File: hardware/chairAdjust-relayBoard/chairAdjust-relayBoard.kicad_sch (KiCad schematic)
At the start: 51 parts, among them J1 Motor_1 + -, J2 Control-Signals, J3 Control-Signals, J4 24V Power, J5 GND Power, J6 12V, GND, J7 Motor_2 + -, K1 RT314A24, K2 RT314A24, K3 RT314A24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

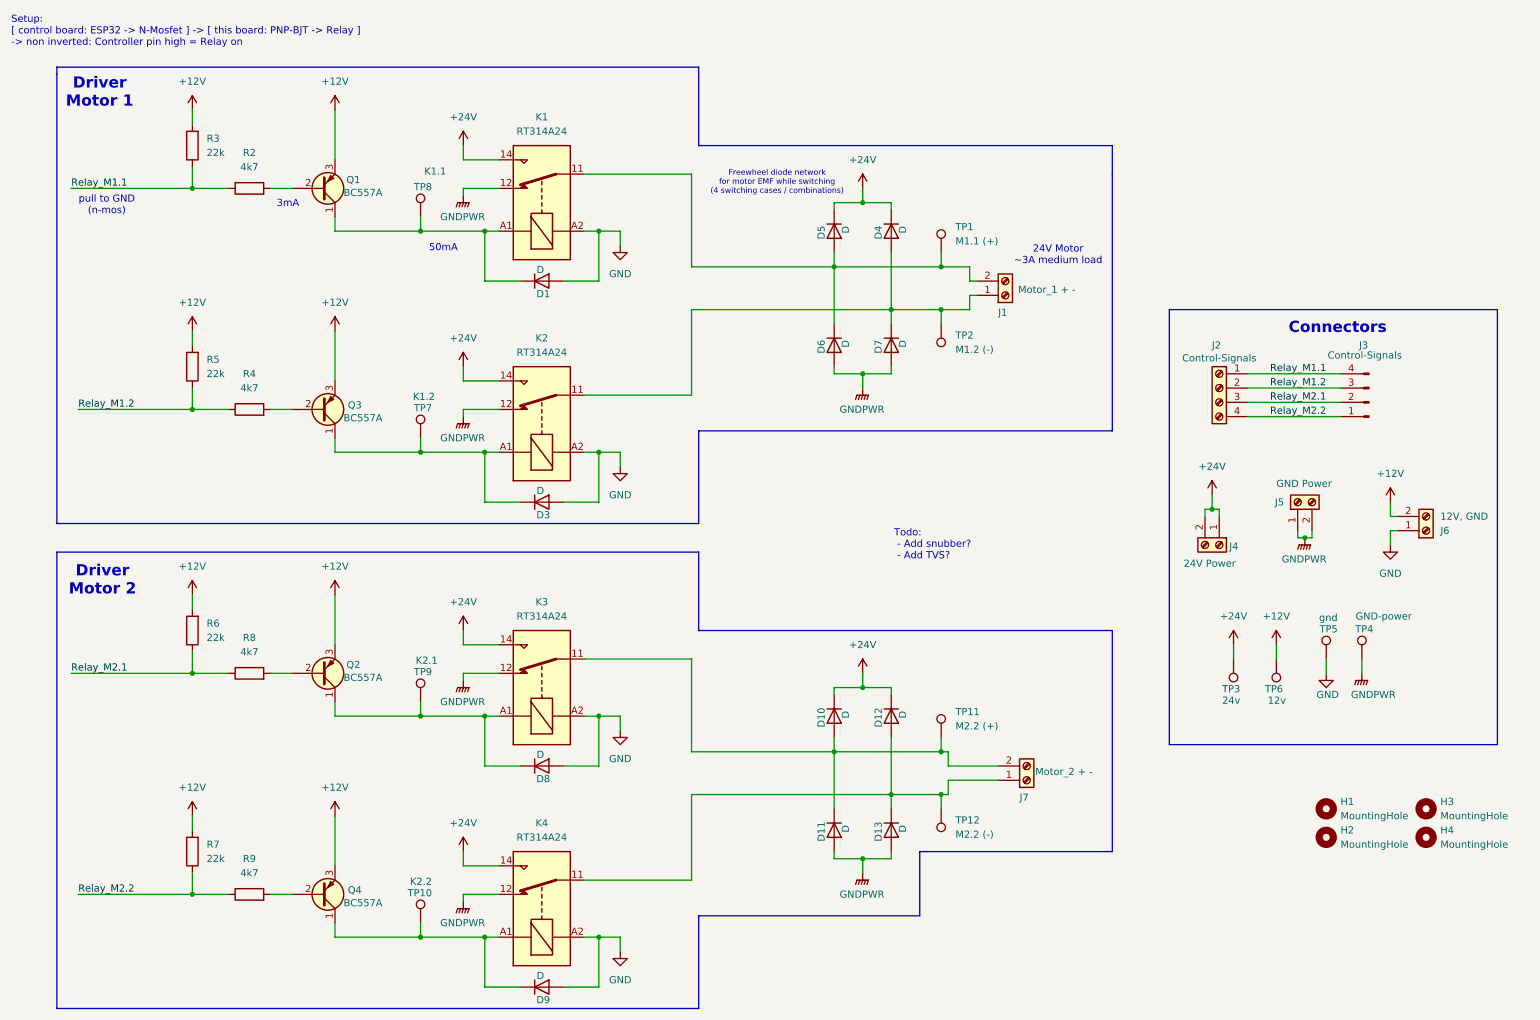
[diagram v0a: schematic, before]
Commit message: pcb: add 3d-model, exports
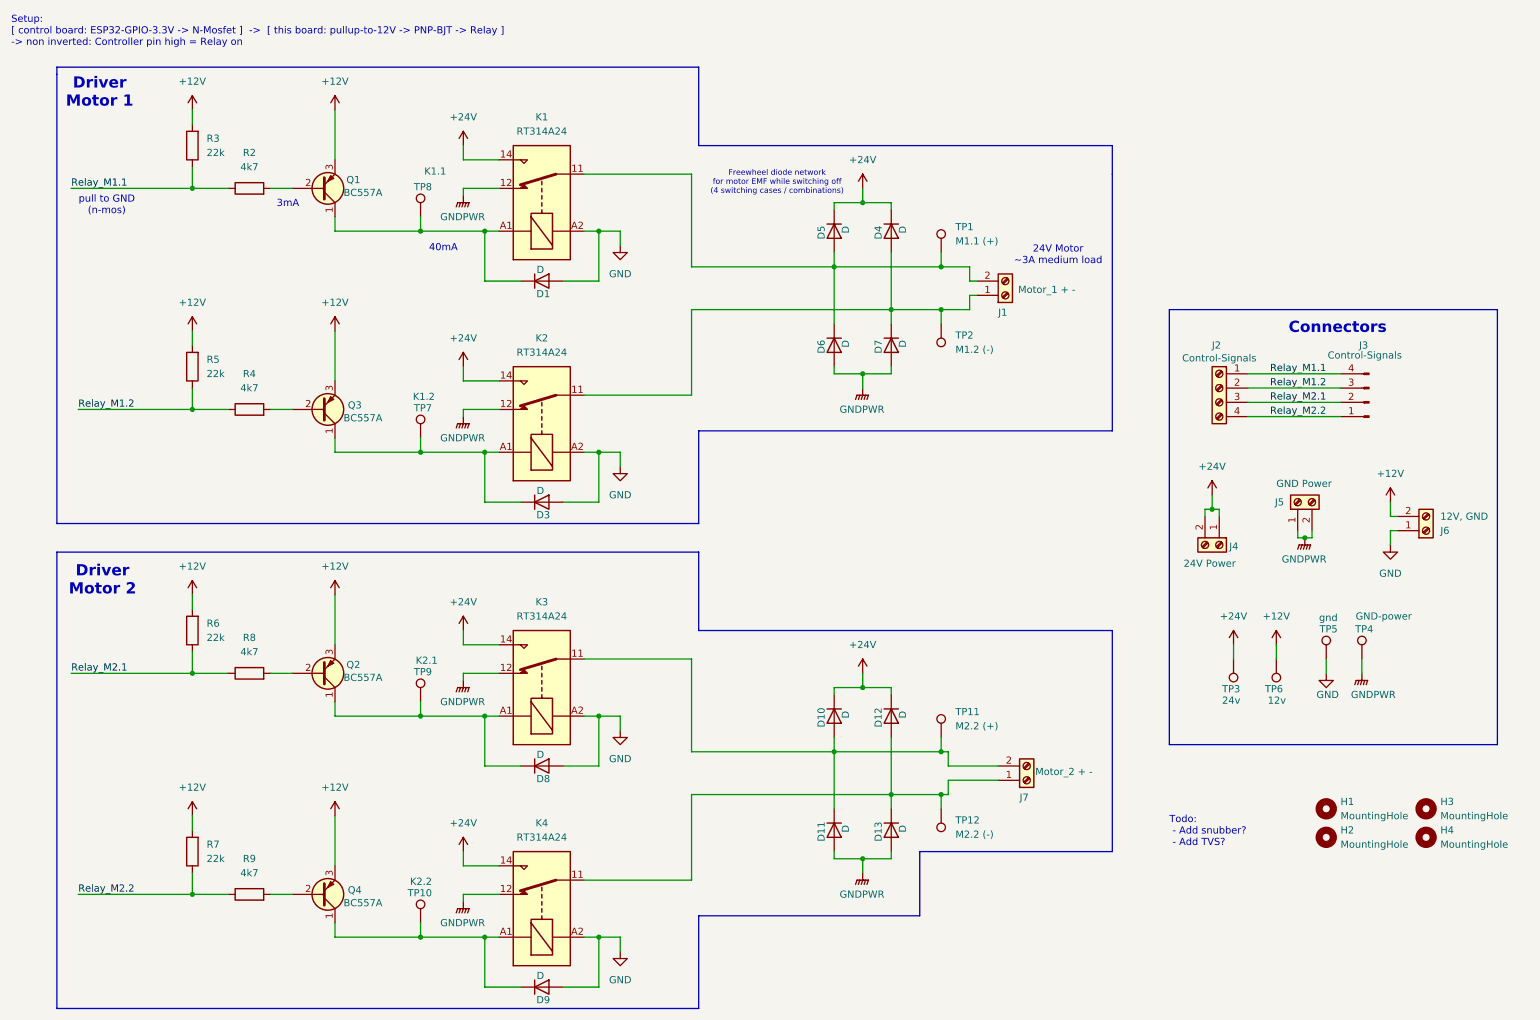
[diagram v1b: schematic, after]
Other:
- note added: "40mA"
- note added: "Freewheel diode network for motor EMF while switching off (4 switching cases / combinations)"
- note added: "Setup: [ control board: ESP32-GPIO-3.3V -> N-Mosfet ] -> [ this board: pullup-to-12V -> PNP-BJT -> Relay ] -> non inverted: Controller pin high = Relay on"
- note removed: "50mA"
- note removed: "Freewheel diode network for motor EMF while switching (4 switching cases / combinations)"
- note removed: "Setup: [ control board: ESP32 -> N-Mosfet ] -> [ this board: PNP-BJT -> Relay ] -> non inverted: Controller pin high = Relay on"
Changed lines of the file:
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@@
 		(date "2024-09-07")
 		(rev "V1.0")
-		(comment 1 "in both direction with protection")
-		(comment 2 "2 motors for chair adjust of armchair")
-		(comment 3 "Relay board for controlling ")
+		(comment 1 "https://github.com/Jonny999999/armchair_fw ")
+		(comment 2 "in both direction with protection")
+		(comment 3 "2 motors for chair adjustment of armchair")
+		(comment 4 "Relay board for controlling ")
 	)
 	(junction
@@
 		)
 	)
-	(text "Setup:\n[ control board: ESP32 -> N-Mosfet ] -> [ this board: PNP-BJT -> Relay ]\n-> non inverted: Controller pin high = Relay on"
+	(text "Setup:\n[ control board: ESP32-GPIO-3.3V -> N-Mosfet ]  ->  [ this board: pullup-to-12V -> PNP-BJT -> Relay ]\n-> non inverted: Controller pin high = Relay on"
 		(exclude_from_sim no)
 		(at 13.462 16.51 0)
@@
 		)
 	)
-	(text "50mA\n"
+	(text "40mA\n"
 		(exclude_from_sim no)
 		(at 90.424 55.118 0)
@@
 	(text "Todo: \n - Add snubber?\n - Add TVS?"
 		(exclude_from_sim no)
-		(at 170.688 107.95 0)
+		(at 219.71 159.004 0)
 		(effects
 			(font
@@
 		)
 	)
-	(text "Freewheel diode network\nfor motor EMF while switching\n(4 switching cases / combinations)"
+	(text "Freewheel diode network\nfor motor EMF while switching off\n(4 switching cases / combinations)"
 		(exclude_from_sim no)
 		(at 149.86 43.434 0)

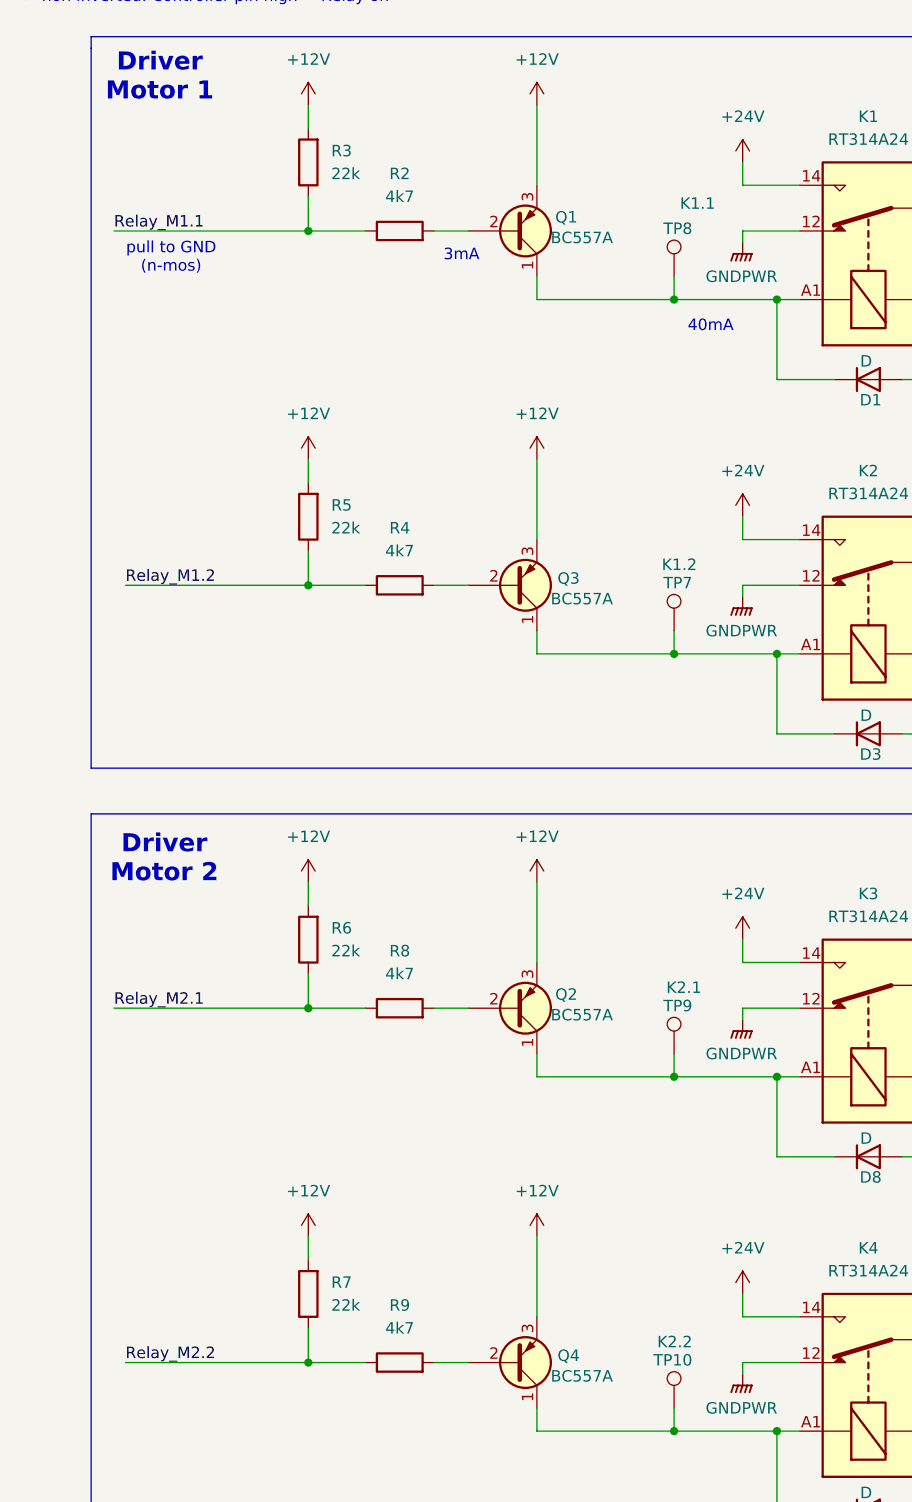
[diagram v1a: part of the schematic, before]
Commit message: Finalize schematic, Add pcb to README
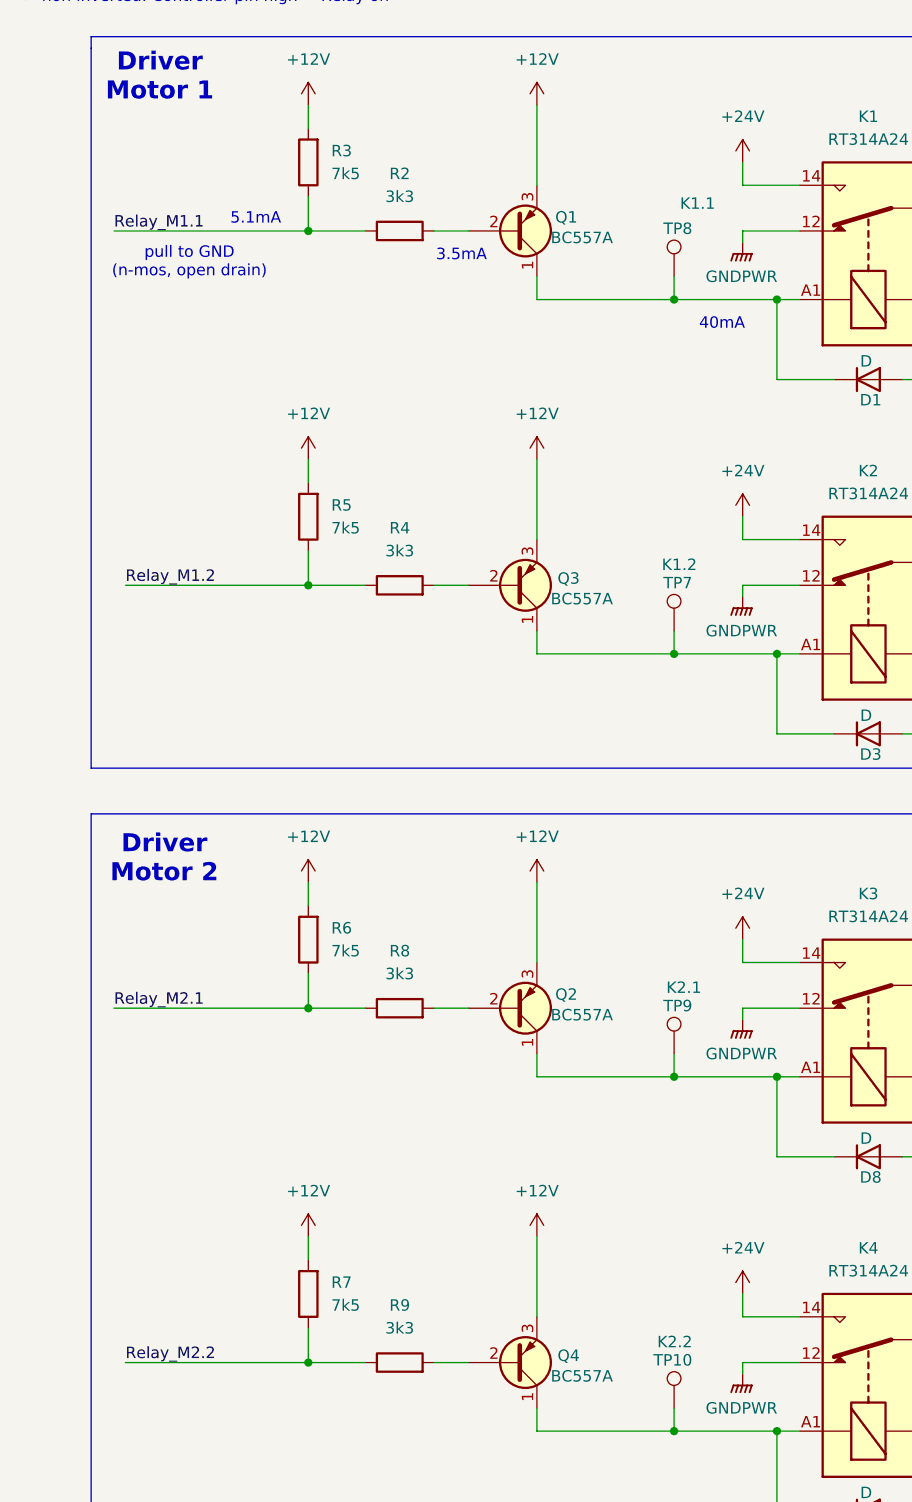
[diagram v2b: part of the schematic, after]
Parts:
- R2, R4, R8, R9: value 4k7 -> 3k3
- R3, R5, R6, R7: value 22k -> 7k5
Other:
- note added: "3.5mA"
- note added: "5.1mA"
- note added: "pull to GND (n-mos, open drain)"
- note removed: "3mA"
- note removed: "pull to GND (n-mos)"
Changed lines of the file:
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@@
 		)
 	)
-	(text "pull to GND\n(n-mos)"
+	(text "pull to GND\n(n-mos, open drain)"
 		(exclude_from_sim no)
-		(at 30.48 47.498 0)
+		(at 32.512 48.006 0)
 		(effects
 			(font
@@
 	(text "40mA\n"
 		(exclude_from_sim no)
-		(at 90.424 55.118 0)
+		(at 91.694 54.864 0)
 		(effects
 			(font
@@
 		)
 	)
-	(text "3mA"
+	(text "5.1mA"
+		(exclude_from_sim no)
+		(at 39.878 43.18 0)
+		(effects
+			(font
+				(size 1.27 1.27)
+			)
+		)
+	)
+	(text "3.5mA"
 		(exclude_from_sim no)
 		(at 62.738 47.244 0)
@@
 			)
 		)
-		(property "Value" "22k"
+		(property "Value" "7k5"
 			(at 48.26 38.0999 0)
 			(effects
@@
 			)
 		)
-		(property "Value" "22k"
+		(property "Value" "7k5"
 			(at 48.26 163.8299 0)
 			(effects
@@
 			)
 		)
-		(property "Value" "4k7"
+		(property "Value" "3k3"
 			(at 55.88 166.37 90)
 			(effects
@@
 			)
 		)
-		(property "Value" "4k7"
+		(property "Value" "3k3"
 			(at 55.88 127 90)
 			(effects
@@
 			)
 		)
-		(property "Value" "22k"
+		(property "Value" "7k5"
 			(at 48.26 124.4599 0)
 			(effects
@@
 			)
 		)
-		(property "Value" "4k7"
+		(property "Value" "3k3"
 			(at 55.88 40.64 90)
 			(effects
@@
 			)
 		)
-		(property "Value" "22k"
+		(property "Value" "7k5"
 			(at 48.26 77.4699 0)
 			(effects
@@
 			)
 		)
-		(property "Value" "4k7"
+		(property "Value" "3k3"
 			(at 55.88 80.01 90)
 			(effects
